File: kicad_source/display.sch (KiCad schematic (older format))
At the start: 19 parts, among them CN3 CONN_01X24, Q1 SI1304BDL

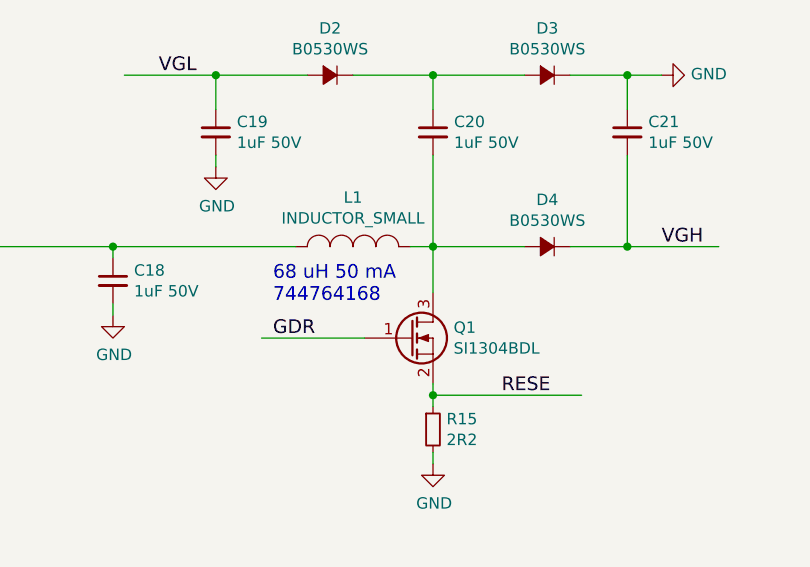
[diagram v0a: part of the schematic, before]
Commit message: added some missing part numbers
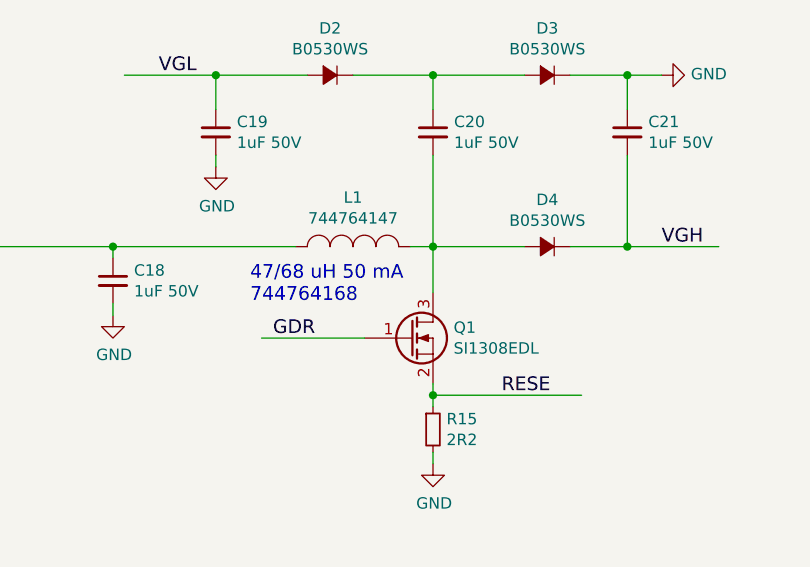
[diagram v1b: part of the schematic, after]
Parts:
- L1: value INDUCTOR_SMALL -> 744764147
- Q1: value SI1304BDL -> SI1308EDL; footprint SOT_TO:SOT-23 -> SOT_TO:SOT-323
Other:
- note added: "47/68 uH 50 mA\n744764168"
- note removed: "68 uH 50 mA\n744764168"
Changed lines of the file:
@@
 P 4250 3750
 F 0 "Q1" H 4440 3796 50  0000 L CNN
-F 1 "SI1304BDL" H 4440 3705 50  0000 L CNN
-F 2 "SOT_TO:SOT-23" H 4450 3850 50  0001 C CNN
+F 1 "SI1308EDL" H 4440 3705 50  0000 L CNN
+F 2 "SOT_TO:SOT-323" H 4450 3850 50  0001 C CNN
 F 3 "" H 4250 3750 50  0000 C CNN
 	1    4250 3750
@@
 P 4000 3350
 F 0 "L1" H 4000 3565 50  0000 C CNN
-F 1 "INDUCTOR_SMALL" H 4000 3474 50  0000 C CNN
+F 1 "744764147" H 4000 3474 50  0000 C CNN
 F 2 "resistors:R_1210" H 4000 3350 50  0001 C CNN
 F 3 "" H 4000 3350 50  0000 C CNN
@@
 Text Notes 6300 5700 0    60   ~ 0
 use display Waveshare 2.9inch e-Paper Module (B)\nhttps://www.waveshare.com/wiki/2.9inch_e-Paper_Module_(B)\nhttps://www.waveshare.com/w/upload/b/bb/2.9inch-e-paper-b-specification.pdf
-Text Notes 3650 3600 0    60   ~ 0
-68 uH 50 mA\n744764168
+Text Notes 3550 3600 0    60   ~ 0
+47/68 uH 50 mA\n744764168
 $EndSCHEMATC

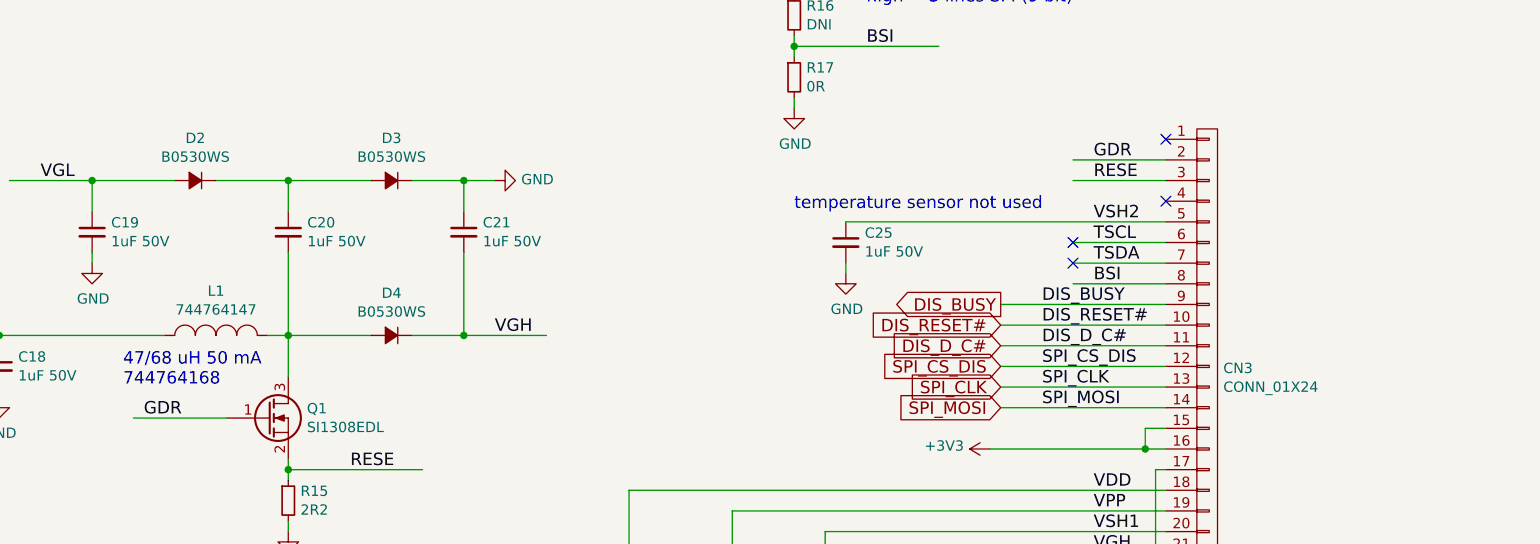
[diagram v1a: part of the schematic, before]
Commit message: optimized parts for BOM costs
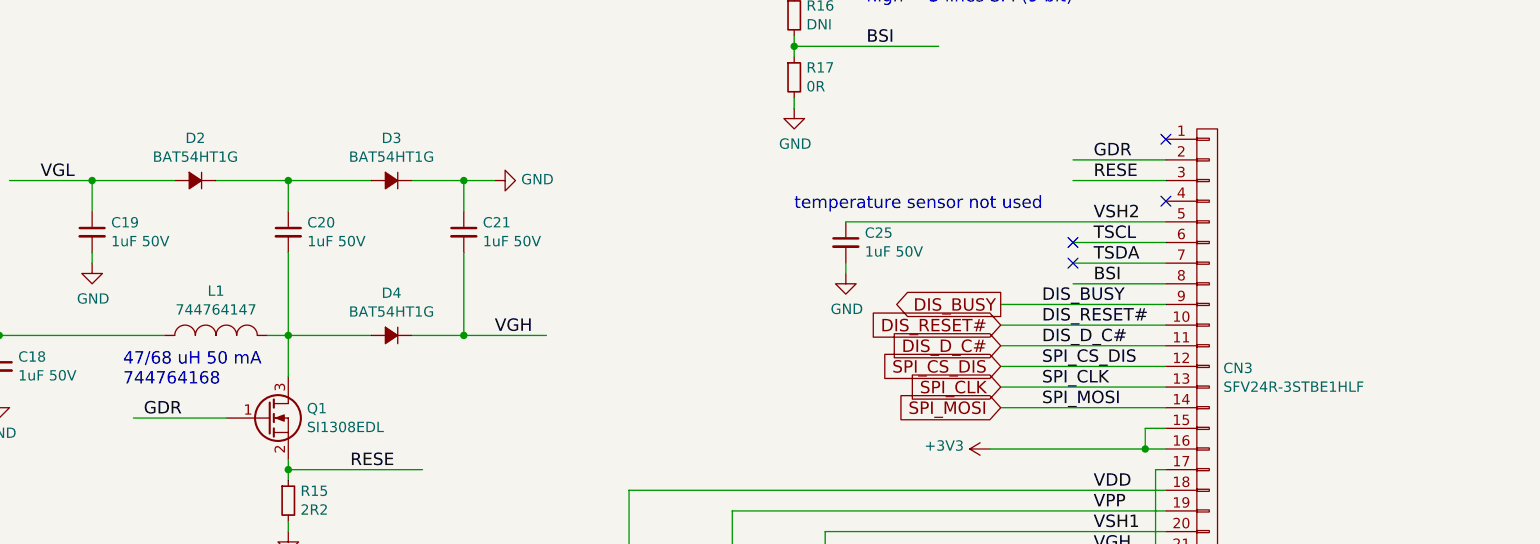
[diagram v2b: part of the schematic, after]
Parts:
- CN3: value CONN_01X24 -> SFV24R-3STBE1HLF
- D2, D3, D4: value B0530WS -> BAT54HT1G
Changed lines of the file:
@@
 P 8800 3550
 F 0 "CN3" H 8878 3591 50  0000 L CNN
-F 1 "CONN_01X24" H 8878 3500 50  0000 L CNN
+F 1 "SFV24R-3STBE1HLF" H 8878 3500 50  0000 L CNN
 F 2 "CON_wuerth:WR-FPC_68712414522" H 8800 3550 50  0001 C CNN
 F 3 "" H 8800 3550 50  0000 C CNN
@@
 P 4850 3350
 F 0 "D4" H 4850 3145 50  0000 C CNN
-F 1 "B0530WS" H 4850 3236 50  0000 C CNN
+F 1 "BAT54HT1G" H 4850 3236 50  0000 C CNN
 F 2 "diodes:SOD-323" V 4850 3350 50  0001 C CNN
 F 3 "" V 4850 3350 50  0000 C CNN
@@
 P 4850 2600
 F 0 "D3" H 4850 2395 50  0000 C CNN
-F 1 "B0530WS" H 4850 2486 50  0000 C CNN
+F 1 "BAT54HT1G" H 4850 2486 50  0000 C CNN
 F 2 "diodes:SOD-323" V 4850 2600 50  0001 C CNN
 F 3 "" V 4850 2600 50  0000 C CNN
@@
 P 3900 2600
 F 0 "D2" H 3900 2395 50  0000 C CNN
-F 1 "B0530WS" H 3900 2486 50  0000 C CNN
+F 1 "BAT54HT1G" H 3900 2486 50  0000 C CNN
 F 2 "diodes:SOD-323" V 3900 2600 50  0001 C CNN
 F 3 "" V 3900 2600 50  0000 C CNN

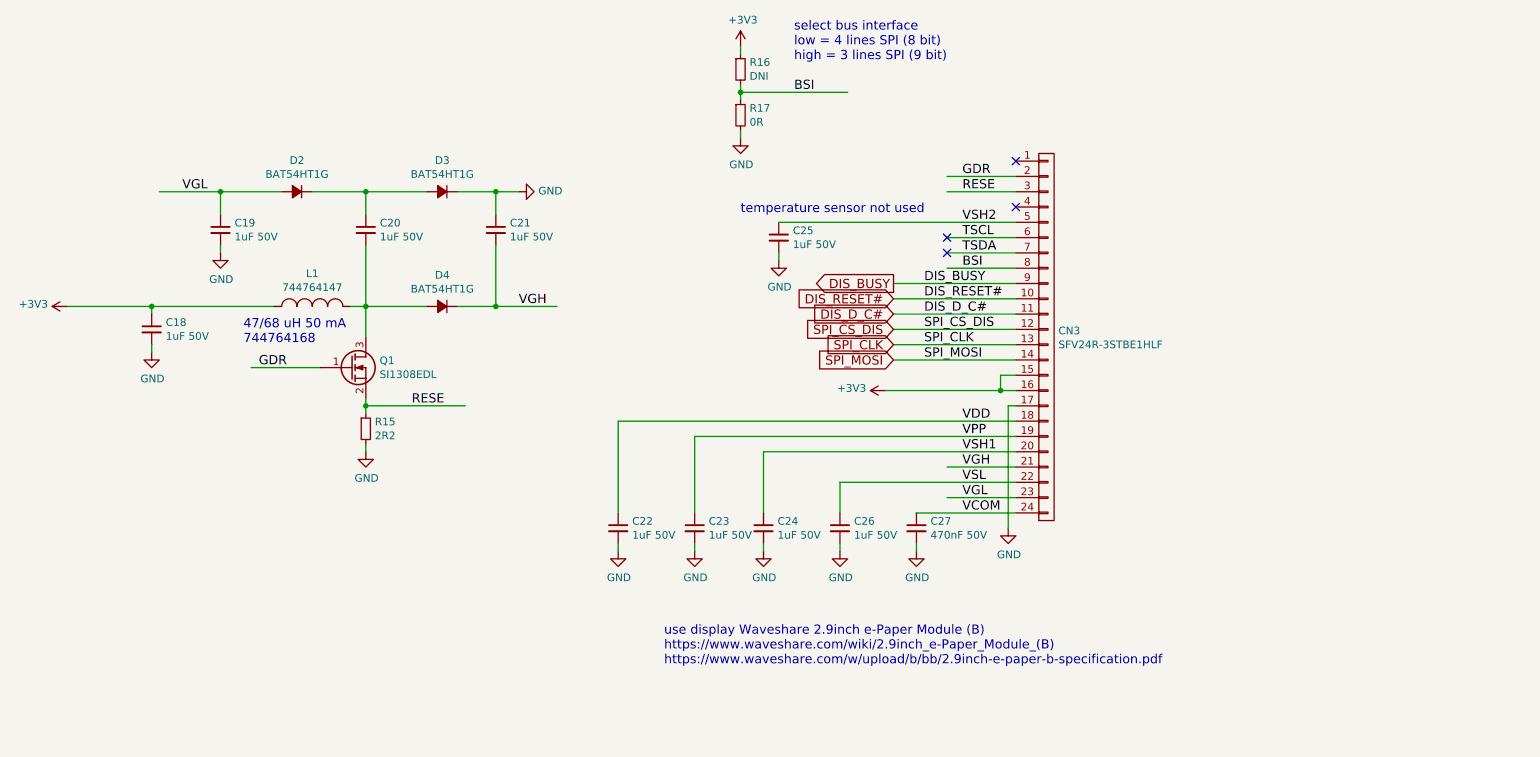
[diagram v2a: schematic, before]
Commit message: added C45 to pin4 of display
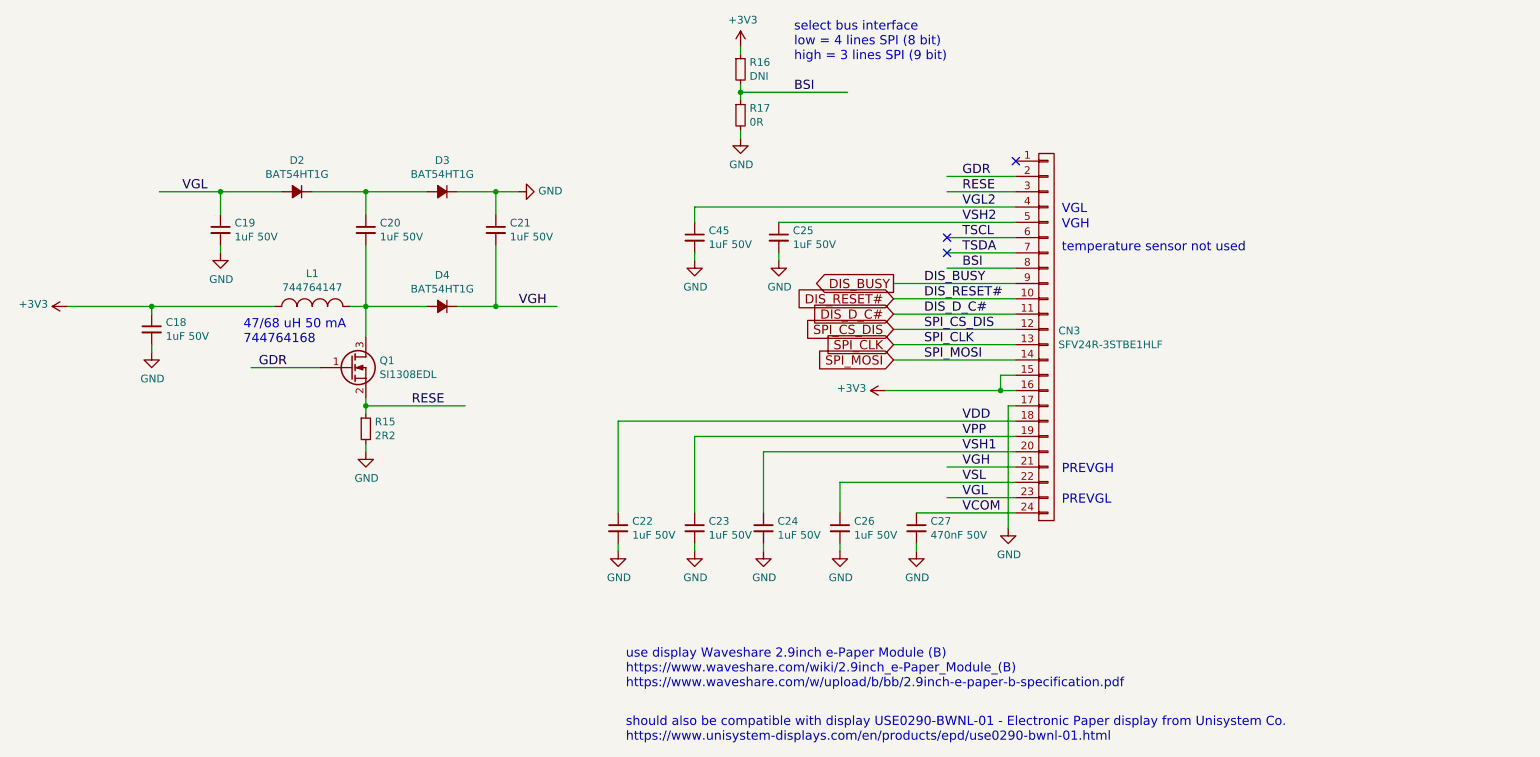
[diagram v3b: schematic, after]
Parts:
- added C45: 1uF 50V, capacitors:C_0603, symbol devices:C_0603
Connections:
- net labels added: VGL2
- wire segments 66 -> 69
- no-connect marks 4 -> 3
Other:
- note added: "PREVGH"
- note added: "PREVGL"
- note added: "VGH"
- note added: "VGL"
- note added: "should also be compatible with display USE0290-BWNL-01 - Electronic Paper display from Unisystem Co.\nhttps://www.unisystem-displays.com/en/products/epd/use0290-bwnl-01.html"
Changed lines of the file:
@@
 Sheet 3 7
 Title "e-paper display"
-Date "2020-05-13"
+Date "2020-07-03"
 Rev "dev_0.1"
 Comp "generationmake"
@@
 Comment4 ""
 $EndDescr
-$Comp
-L mechanical-connectors:CONN_01X24 CN3
-U 1 1 5EC3DC2E
-P 8800 3550
-F 0 "CN3" H 8878 3591 50  0000 L CNN
-F 1 "SFV24R-3STBE1HLF" H 8878 3500 50  0000 L CNN
-F 2 "CON_wuerth:WR-FPC_68712414522" H 8800 3550 50  0001 C CNN
-F 3 "" H 8800 3550 50  0000 C CNN
-	1    8800 3550
-	1    0    0    -1
-$EndComp
 NoConn ~ 8600 2400
-NoConn ~ 8600 2700
 Wire Wire Line
 	8150 2500 8600 2500
@@
 NoConn ~ 8150 2900
 NoConn ~ 8150 3000
-Text Notes 6800 2750 0    60   ~ 0
+Text Notes 8900 3000 0    60   ~ 0
 temperature sensor not used
 $Comp
@@
 Text GLabel 7800 3400 0    60   Input ~ 0
 DIS_D_C#
-Text Notes 6300 5700 0    60   ~ 0
+Text Notes 6050 5850 0    60   ~ 0
 use display Waveshare 2.9inch e-Paper Module (B)\nhttps://www.waveshare.com/wiki/2.9inch_e-Paper_Module_(B)\nhttps://www.waveshare.com/w/upload/b/bb/2.9inch-e-paper-b-specification.pdf
 Text Notes 3550 3600 0    60   ~ 0
 47/68 uH 50 mA\n744764168
+Text Notes 6050 6200 0    60   ~ 0
+should also be compatible with display USE0290-BWNL-01 - Electronic Paper display from Unisystem Co.\nhttps://www.unisystem-displays.com/en/products/epd/use0290-bwnl-01.html
+Text Notes 8900 2750 0    60   ~ 0
+VGL
+Text Notes 8900 2850 0    60   ~ 0
+VGH
+Text Notes 8900 4450 0    60   ~ 0
+PREVGH
+Text Notes 8900 4650 0    60   ~ 0
+PREVGL
+$Comp
+L devices:C_0603 C45
+U 1 1 5EFFDBE8
+P 6500 2900
+F 0 "C45" H 6592 2946 50  0000 L CNN
+F 1 "1uF 50V" H 6592 2855 50  0000 L CNN
+F 2 "capacitors:C_0603" H 6500 2750 50  0001 C CNN
+F 3 "" H 6500 2900 50  0000 C CNN
+	1    6500 2900
+	1    0    0    -1
+$EndComp
+$Comp
+L power-supply:GND #PWR086
+U 1 1 5EFFDE70
+P 6500 3050
+F 0 "#PWR086" H 6500 2800 50  0001 C CNN
+F 1 "GND" H 6505 2877 50  0000 C CNN
+F 2 "" H 6500 3050 50  0000 C CNN
+F 3 "" H 6500 3050 50  0000 C CNN
+	1    6500 3050
+	1    0    0    -1
+$EndComp
+$Comp
+L mechanical-connectors:CONN_01X24 CN3
+U 1 1 5EC3DC2E
+P 8800 3550
+F 0 "CN3" H 8878 3591 50  0000 L CNN
+F 1 "SFV24R-3STBE1HLF" H 8878 3500 50  0000 L CNN
+F 2 "CON_wuerth:WR-FPC_68712414522" H 8800 3550 50  0001 C CNN
+F 3 "" H 8800 3550 50  0000 C CNN
+	1    8800 3550
+	1    0    0    -1
+$EndComp
+Wire Wire Line
+	8600 2700 6500 2700
+Wire Wire Line
+	6500 2700 6500 2800
+Wire Wire Line
+	6500 3000 6500 3050
+Text Label 8250 2700 0    60   ~ 0
+VGL2
 $EndSCHEMATC
